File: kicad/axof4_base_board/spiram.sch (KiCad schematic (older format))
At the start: 3 parts, among them U2 23LC1024-I_SN

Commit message: backup
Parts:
- C23: symbol Device:C_Small -> axof4_base_board-rescue:C_Small-Device
- R24: symbol Device:R -> axof4_base_board-rescue:R-Device
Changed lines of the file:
@@
 $Descr A4 11693 8268
 encoding utf-8
-Sheet 4 4
+Sheet 4 5
 Title ""
 Date ""
@@
 U 1 1 5ECDC1BB
 P 3700 3550
+AR Path="/5ECDA234/5ECDC1BB" Ref="U2"  Part="1"
+AR Path="/5ED86ED4/5ECDC1BB" Ref="U?"  Part="1"
 F 0 "U2" H 5300 3937 60  0000 C CNN
 F 1 "23LC1024-I_SN" H 5300 3831 60  0000 C CNN
@@
 $EndComp
 $Comp
-L power:+3.3V #PWR026
+L axof4_base_board-rescue:+3.3V-power #PWR026
 U 1 1 5ECDCA2B
 P 7150 3400
+AR Path="/5ECDA234/5ECDCA2B" Ref="#PWR026"  Part="1"
+AR Path="/5ED86ED4/5ECDCA2B" Ref="#PWR?"  Part="1"
 F 0 "#PWR026" H 7150 3250 50  0001 C CNN
 F 1 "+3.3V" H 7165 3573 50  0000 C CNN
@@
 	6900 3750 7150 3750
 $Comp
-L power:GND #PWR024
-U 1 1 5ECDDAD6
+L axof4_base_board-rescue:GND-power #PWR024
+U 1 1 5EDD81C1
 P 3500 4050
+AR Path="/5ECDA234/5EDD81C1" Ref="#PWR024"  Part="1"
+AR Path="/5ED86ED4/5EDD81C1" Ref="#PWR?"  Part="1"
 F 0 "#PWR024" H 3500 3800 50  0001 C CNN
 F 1 "GND" H 3505 3877 50  0000 C CNN
@@
 Connection ~ 7150 3550
 $Comp
-L Device:R R24
+L axof4_base_board-rescue:R-Device R24
 U 1 1 5ECDE811
 P 3500 3300
+AR Path="/5ECDA234/5ECDE811" Ref="R24"  Part="1"
+AR Path="/5ED86ED4/5ECDE811" Ref="R?"  Part="1"
 F 0 "R24" H 3350 3250 50  0000 C CNN
 F 1 "10k" V 3500 3300 50  0000 C CNN
@@
 $EndComp
 $Comp
-L power:+3.3V #PWR023
-U 1 1 5ECDF67F
+L axof4_base_board-rescue:+3.3V-power #PWR023
+U 1 1 5EDD81C2
 P 3500 3100
+AR Path="/5ECDA234/5EDD81C2" Ref="#PWR023"  Part="1"
+AR Path="/5ED86ED4/5EDD81C2" Ref="#PWR?"  Part="1"
 F 0 "#PWR023" H 3500 2950 50  0001 C CNN
 F 1 "+3.3V" H 3500 3250 50  0000 C CNN
@@
 	3100 3550 3500 3550
 $Comp
-L Device:C_Small C23
+L axof4_base_board-rescue:C_Small-Device C23
 U 1 1 5ECE0CFC
 P 6950 3300
+AR Path="/5ECDA234/5ECE0CFC" Ref="C23"  Part="1"
+AR Path="/5ED86ED4/5ECE0CFC" Ref="C?"  Part="1"
 F 0 "C23" H 7100 3250 50  0000 R CNN
 F 1 "100n" H 7150 3350 50  0000 R CNN
@@
 $EndComp
 $Comp
-L power:GND #PWR025
+L axof4_base_board-rescue:GND-power #PWR025
 U 1 1 5ECE192A
 P 6600 3100
+AR Path="/5ECDA234/5ECE192A" Ref="#PWR025"  Part="1"
+AR Path="/5ED86ED4/5ECE192A" Ref="#PWR?"  Part="1"
 F 0 "#PWR025" H 6600 2850 50  0001 C CNN
 F 1 "GND" H 6605 2927 50  0000 C CNN
@@
 	6600 3050 6600 3100
 $Comp
-L power:+3.3V #PWR022
+L axof4_base_board-rescue:+3.3V-power #PWR022
 U 1 1 5ECE6440
 P 3150 3900
+AR Path="/5ECDA234/5ECE6440" Ref="#PWR022"  Part="1"
+AR Path="/5ED86ED4/5ECE6440" Ref="#PWR?"  Part="1"
 F 0 "#PWR022" H 3150 3750 50  0001 C CNN
 F 1 "+3.3V" H 3150 4050 50  0000 C CNN

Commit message: kicad pcb backup, hohum axoctrl study
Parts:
- added J8: SPI2_HEADER, symbol Connector_Generic:Conn_02x03_Odd_Even
- added R35: 10k, Resistor_SMD:R_1206_3216Metric_Pad1.42x1.75mm_HandSolder, symbol axof4_base_board-rescue:R-Device
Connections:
- net +3V3: now also J8.2 (Pin_2), R35.2
- net GND: now also J8.6 (Pin_6)
- net SPIRAM_MISO: now also J8.1 (Pin_1)
- net SPIRAM_MOSI-VGA_PIXEL: now also J8.4 (Pin_4)
- net SPIRAM_SCK: now also J8.3 (Pin_3)
- new net SPI2_SOFT_NSS: J8.5 (Pin_5), R35.1
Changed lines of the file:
@@
 Wire Wire Line
 	3500 3100 3500 3150
+$Comp
+L Connector_Generic:Conn_02x03_Odd_Even J?
+U 1 1 603C4C1A
+P 4950 5500
+AR Path="/603C4C1A" Ref="J?"  Part="1"
+AR Path="/5ECDA234/603C4C1A" Ref="J8"  Part="1"
+F 0 "J8" H 5000 5817 50  0000 C CNN
+F 1 "SPI2_HEADER" H 5000 5726 50  0000 C CNN
+F 2 "" H 4950 5500 50  0001 C CNN
+F 3 "~" H 4950 5500 50  0001 C CNN
+	1    4950 5500
+	1    0    0    -1
+$EndComp
+$Comp
+L axof4_base_board-rescue:+3.3V-power #PWR?
+U 1 1 603C4C20
+P 5350 5250
+AR Path="/603C4C20" Ref="#PWR?"  Part="1"
+AR Path="/5EFC127A/603C4C20" Ref="#PWR?"  Part="1"
+AR Path="/5ECDA234/603C4C20" Ref="#PWR044"  Part="1"
+F 0 "#PWR044" H 5350 5100 50  0001 C CNN
+F 1 "+3.3V" H 5365 5423 50  0000 C CNN
+F 2 "" H 5350 5250 50  0001 C CNN
+F 3 "" H 5350 5250 50  0001 C CNN
+	1    5350 5250
+	1    0    0    -1
+$EndComp
+Text GLabel 4700 5500 0    50   Input ~ 0
+SPIRAM_SCK
+Text GLabel 4700 5400 0    50   Input ~ 0
+SPIRAM_MISO
+Text GLabel 5300 5500 2    50   Input ~ 0
+SPIRAM_MOSI-VGA_PIXEL
+Wire Wire Line
+	5250 5500 5300 5500
+$Comp
+L power:GND #PWR?
+U 1 1 603C4C3C
+P 5300 5650
+AR Path="/603C4C3C" Ref="#PWR?"  Part="1"
+AR Path="/5ECDA234/603C4C3C" Ref="#PWR043"  Part="1"
+F 0 "#PWR043" H 5300 5400 50  0001 C CNN
+F 1 "GND" H 5305 5477 50  0000 C CNN
+F 2 "" H 5300 5650 50  0001 C CNN
+F 3 "" H 5300 5650 50  0001 C CNN
+	1    5300 5650
+	1    0    0    -1
+$EndComp
+Wire Wire Line
+	5300 5650 5300 5600
+Wire Wire Line
+	5300 5600 5250 5600
+Text GLabel 4000 5600 0    50   Input ~ 0
+SPI2_SOFT_NSS
+Wire Wire Line
+	4700 5400 4750 5400
+Wire Wire Line
+	4750 5500 4700 5500
+Wire Wire Line
+	4000 5600 4050 5600
+$Comp
+L axof4_base_board-rescue:R-Device R35
+U 1 1 603CF6F9
+P 4050 5250
+AR Path="/5ECDA234/603CF6F9" Ref="R35"  Part="1"
+AR Path="/5ED86ED4/603CF6F9" Ref="R?"  Part="1"
+AR Path="/5EE2DB57/603CF6F9" Ref="R?"  Part="1"
+AR Path="/603CF6F9" Ref="R?"  Part="1"
+F 0 "R35" H 3900 5200 50  0000 C CNN
+F 1 "10k" V 4050 5250 50  0000 C CNN
+F 2 "Resistor_SMD:R_1206_3216Metric_Pad1.42x1.75mm_HandSolder" V 3980 5250 50  0001 C CNN
+F 3 "~" H 4050 5250 50  0001 C CNN
+	1    4050 5250
+	-1   0    0    1
+$EndComp
+$Comp
+L axof4_base_board-rescue:+3.3V-power #PWR042
+U 1 1 603CF6FF
+P 4050 5050
+AR Path="/5ECDA234/603CF6FF" Ref="#PWR042"  Part="1"
+AR Path="/5ED86ED4/603CF6FF" Ref="#PWR?"  Part="1"
+AR Path="/5EE2DB57/603CF6FF" Ref="#PWR?"  Part="1"
+AR Path="/603CF6FF" Ref="#PWR?"  Part="1"
+F 0 "#PWR042" H 4050 4900 50  0001 C CNN
+F 1 "+3.3V" H 4050 5200 50  0000 C CNN
+F 2 "" H 4050 5050 50  0001 C CNN
+F 3 "" H 4050 5050 50  0001 C CNN
+	1    4050 5050
+	1    0    0    -1
+$EndComp
+Wire Wire Line
+	4050 5050 4050 5100
+Wire Wire Line
+	4050 5400 4050 5600
+Connection ~ 4050 5600
+Wire Wire Line
+	4050 5600 4750 5600
+Wire Wire Line
+	5350 5250 5350 5400
+Wire Wire Line
+	5350 5400 5250 5400
 $EndSCHEMATC

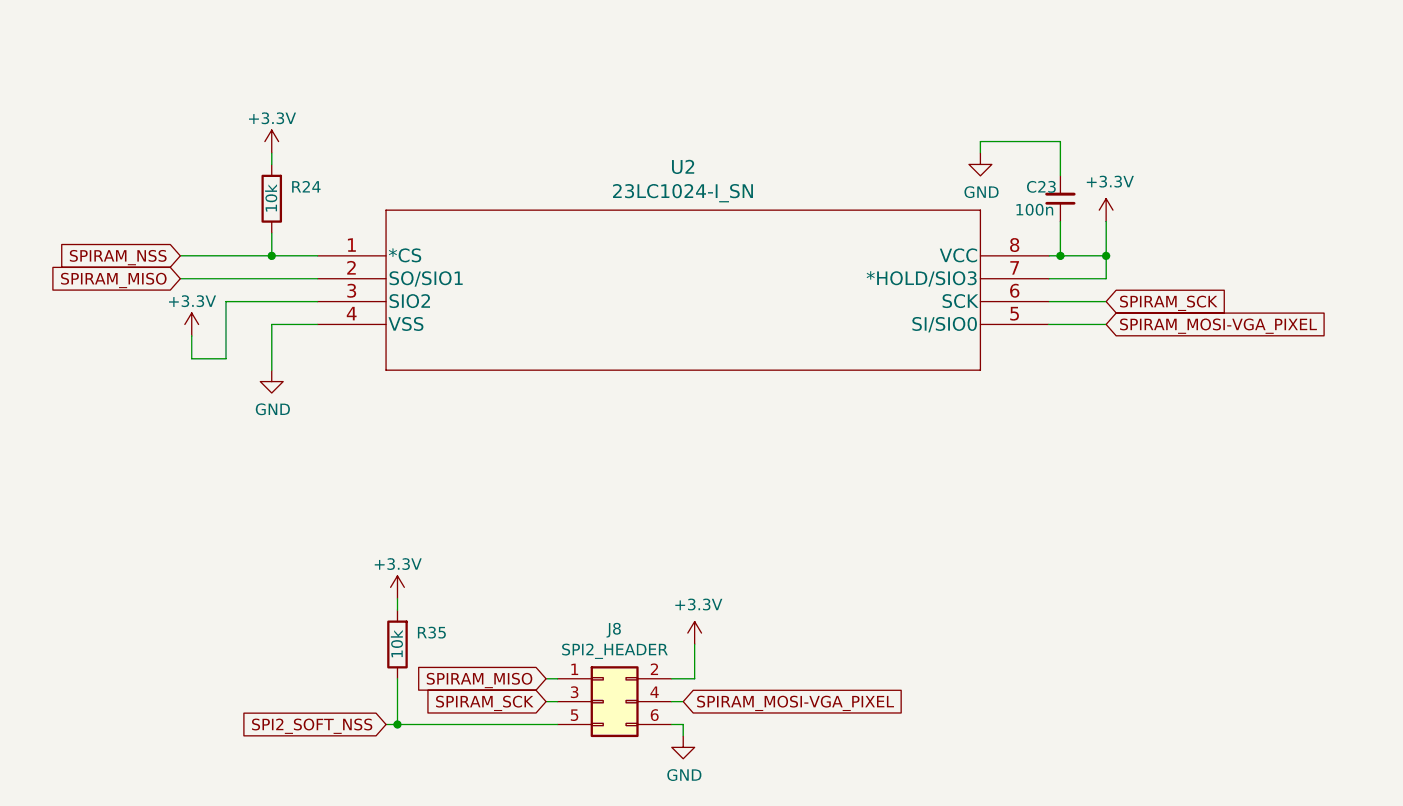
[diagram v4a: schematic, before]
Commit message: rollback kicad project to use STM32F4DISCOVERY
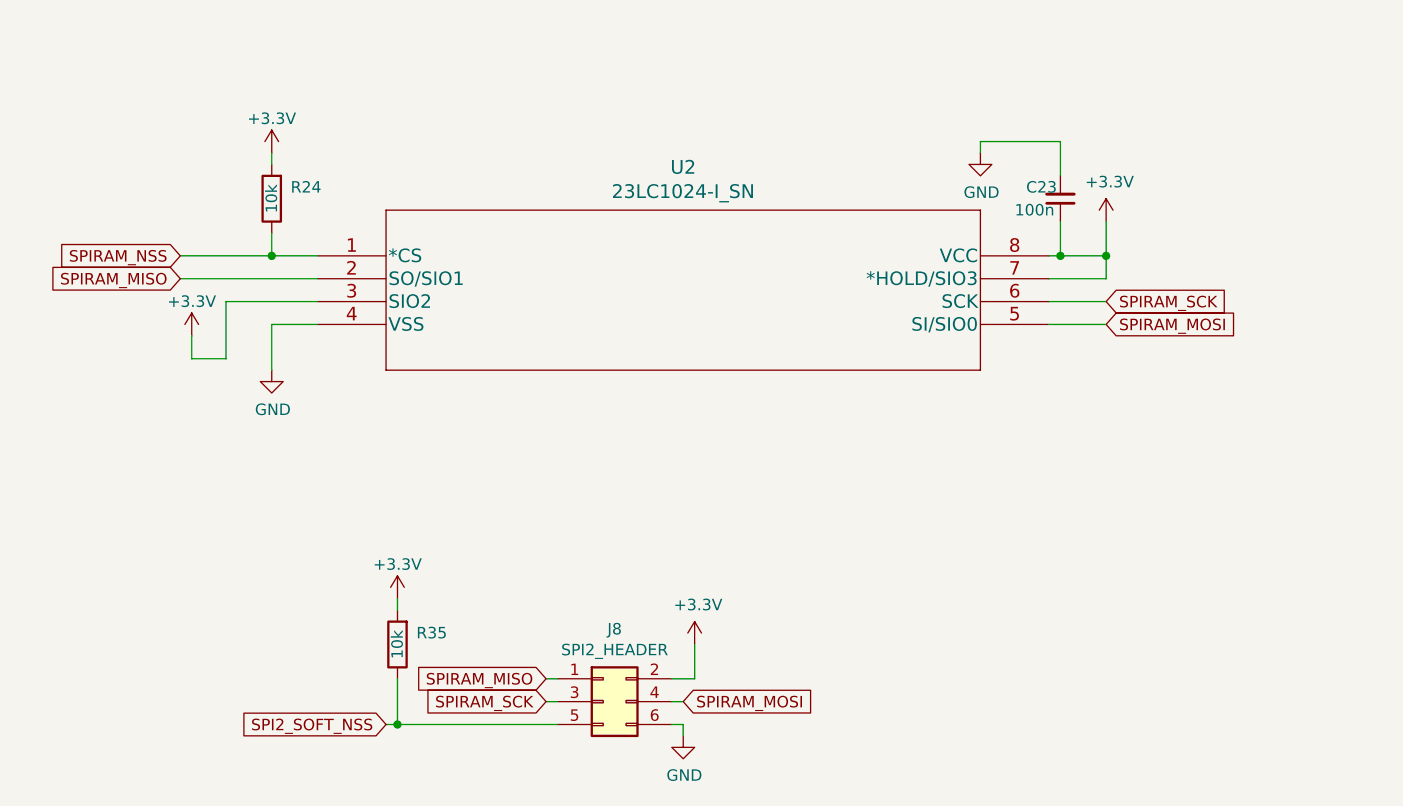
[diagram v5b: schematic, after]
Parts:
- C23: footprint Capacitor_SMD:C_1206_3216Metric_Pad1.42x1.75mm_HandSolder -> Capacitor_SMD:C_0603_1608Metric
- J8: footprint (none) -> Connector_PinHeader_2.54mm:PinHeader_2x03_P2.54mm_Vertical
- R24, R35: footprint Resistor_SMD:R_1206_3216Metric_Pad1.42x1.75mm_HandSolder -> Resistor_SMD:R_0603_1608Metric
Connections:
- net SPIRAM_MOSI-VGA_PIXEL renamed SPIRAM_MOSI
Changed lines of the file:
@@
 SPIRAM_MISO
 Text GLabel 7150 3850 2    50   Input ~ 0
-SPIRAM_MOSI-VGA_PIXEL
+SPIRAM_MOSI
 $Comp
 L 23LC1024:23LC1024-I_SN U2
@@
 F 0 "R24" H 3350 3250 50  0000 C CNN
 F 1 "10k" V 3500 3300 50  0000 C CNN
-F 2 "Resistor_SMD:R_1206_3216Metric_Pad1.42x1.75mm_HandSolder" V 3430 3300 50  0001 C CNN
+F 2 "Resistor_SMD:R_0603_1608Metric" V 3430 3300 50  0001 C CNN
 F 3 "~" H 3500 3300 50  0001 C CNN
 	1    3500 3300
@@
 F 0 "C23" H 7100 3250 50  0000 R CNN
 F 1 "100n" H 7150 3350 50  0000 R CNN
-F 2 "Capacitor_SMD:C_1206_3216Metric_Pad1.42x1.75mm_HandSolder" H 6950 3300 50  0001 C CNN
+F 2 "Capacitor_SMD:C_0603_1608Metric" H 6950 3300 50  0001 C CNN
 F 3 "~" H 6950 3300 50  0001 C CNN
 	1    6950 3300
@@
 F 0 "J8" H 5000 5817 50  0000 C CNN
 F 1 "SPI2_HEADER" H 5000 5726 50  0000 C CNN
-F 2 "" H 4950 5500 50  0001 C CNN
+F 2 "Connector_PinHeader_2.54mm:PinHeader_2x03_P2.54mm_Vertical" H 4950 5500 50  0001 C CNN
 F 3 "~" H 4950 5500 50  0001 C CNN
 	1    4950 5500
@@
 SPIRAM_MISO
 Text GLabel 5300 5500 2    50   Input ~ 0
-SPIRAM_MOSI-VGA_PIXEL
+SPIRAM_MOSI
 Wire Wire Line
 	5250 5500 5300 5500
@@
 F 0 "R35" H 3900 5200 50  0000 C CNN
 F 1 "10k" V 4050 5250 50  0000 C CNN
-F 2 "Resistor_SMD:R_1206_3216Metric_Pad1.42x1.75mm_HandSolder" V 3980 5250 50  0001 C CNN
+F 2 "Resistor_SMD:R_0603_1608Metric" V 3980 5250 50  0001 C CNN
 F 3 "~" H 4050 5250 50  0001 C CNN
 	1    4050 5250
